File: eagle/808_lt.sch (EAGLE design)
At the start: 58 parts, among them IC1 TL071P, IC2 TL072P, Q1 2N3904, Q2 2N3906, Q3 2N3904, SW8 MSS42_SW_4PDT

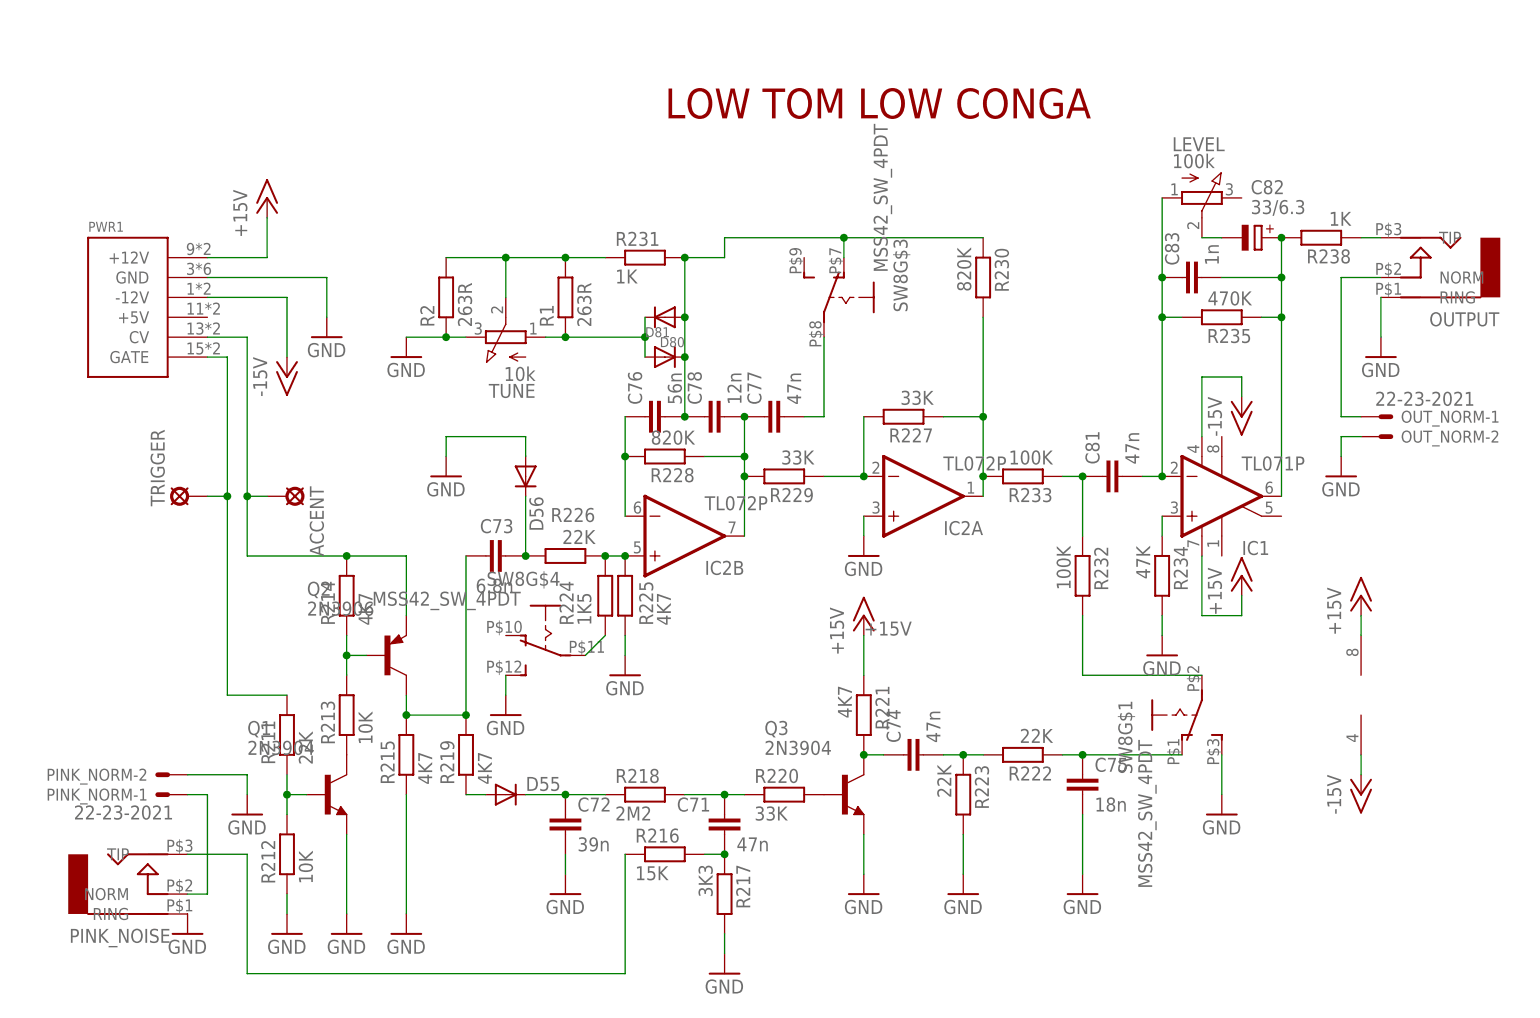
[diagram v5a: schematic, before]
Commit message: corrected 4pdt toggle body size
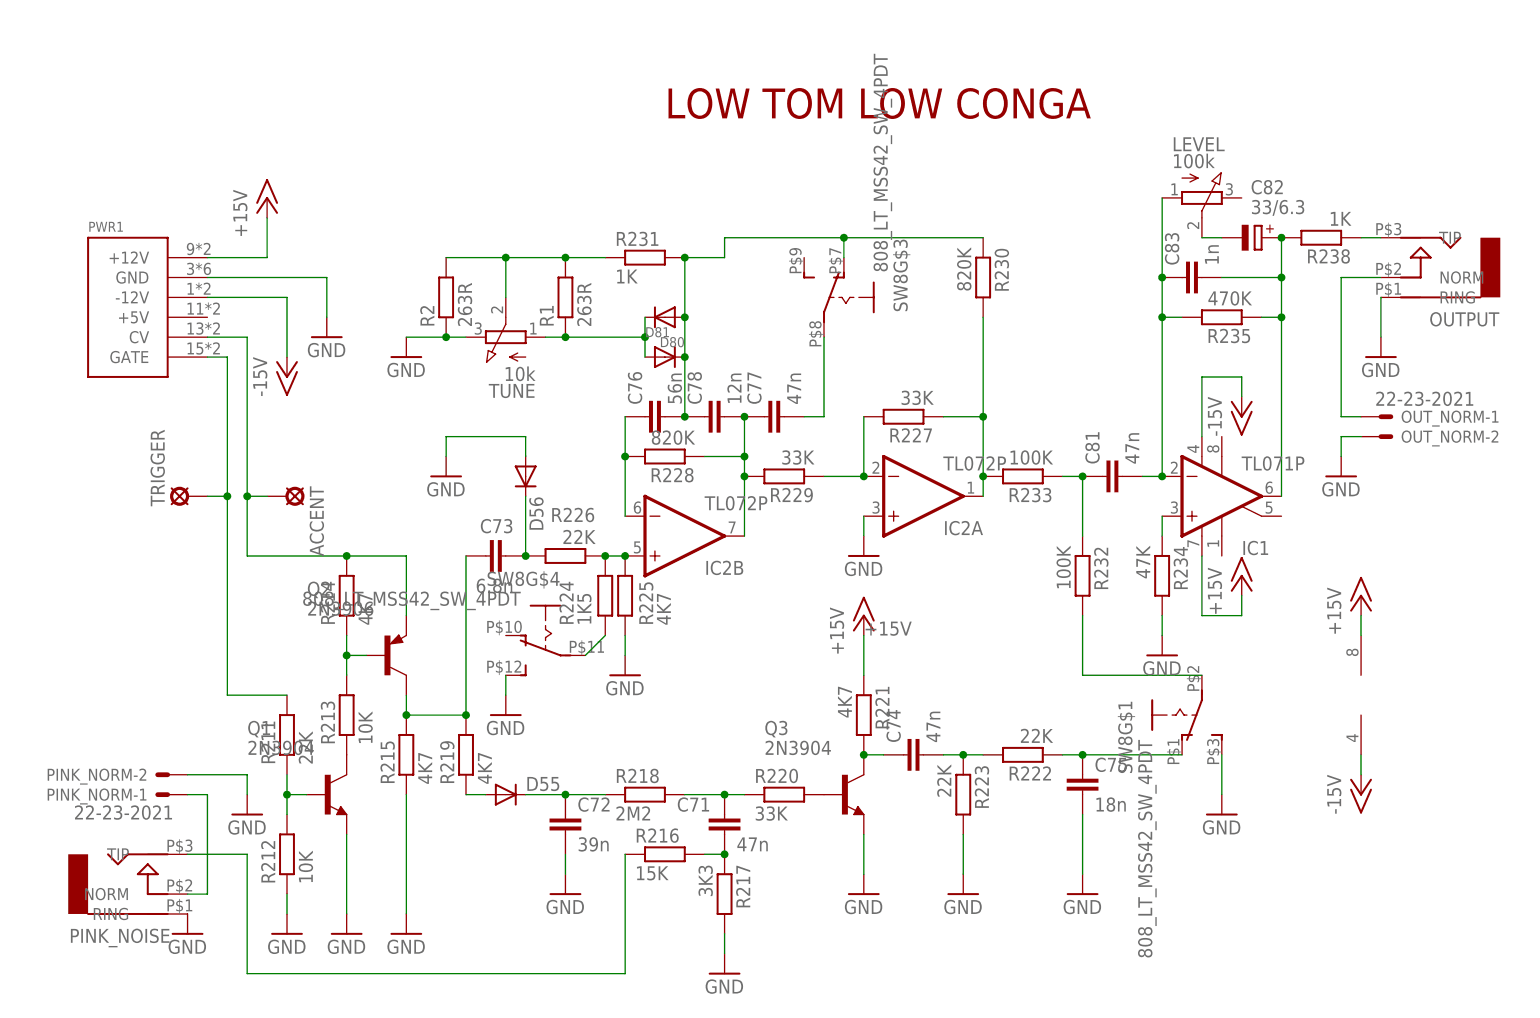
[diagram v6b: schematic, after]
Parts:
- SW8: value MSS42_SW_4PDT -> 808_LT_MSS42_SW_4PDT; device 808_lt:MSS42_SW_4PDT -> 808_lt:808_LT_MSS42_SW_4PDT
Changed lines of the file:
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@@
 <part name="D56" library="adafruit" deviceset="DIODE" device="DO-1N4148"/>
 <part name="V54" library="supply1" deviceset="GND" device=""/>
-<part name="SW8" library="808_lt" deviceset="MSS42_SW_4PDT" device=""/>
+<part name="SW8" library="808_lt" deviceset="808_LT_MSS42_SW_4PDT" device=""/>
 <part name="Q1" library="transistor-npn" deviceset="2N3904" device=""/>
 <part name="Q2" library="transistor-pnp" deviceset="2N3906" device=""/>
